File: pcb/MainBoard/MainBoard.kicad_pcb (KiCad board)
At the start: 2 copper layers, 47 parts, among them P1 Camera pot 1, P2 Camera pot 2, P3 Motor controller, P4 Motor battery, P5 Steering connector, P6 Arduino battery, SW1 OnOffDoubleSwitch, U1 arduino_mini, U2 notgate_74HCT04, U3 arduino_mini

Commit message: PCB design finished
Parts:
- removed C_BULK_1, C_BULK_2, C_BULK_3: 10-100uF, Capacitors_ThroughHole:C_Radial_D6.3_L11.2_P2.5
- removed C_BULK_10, C_BULK_11, C_BULK_4, C_BULK_5, C_BULK_6, C_BULK_7, C_BULK_8, C_BULK_9: 10-100uF, Capacitors_SMD:C_1206_HandSoldering
- removed C_PWR_3, C_PWR_4: C, Capacitors_ThroughHole:C_Radial_D6.3_L11.2_P2.5
- removed U1, U3: arduino_mini, arduino:arduino_mini
- removed U2: notgate_74HCT04, Housings_SOIC:SOIC-14_3.9x8.7mm_Pitch1.27mm
- added ARD1: arduino_mini, arduino:arduino_mini, B.Cu at (79.8, 76.2)
- added ARD2: arduino_mini, arduino:arduino_mini, B.Cu at (114.8, 77.3)
- added C_3VBULK_1: 10-100uF, Capacitors_SMD:C_1206_HandSoldering, B.Cu at (90.7, 50.7)
- added C_3VBULK_2: 10-100uF, Capacitors_SMD:C_1206_HandSoldering, B.Cu at (90.7, 54.3)
- added C_5VBULK_1: 10-100uF, Capacitors_ThroughHole:C_Radial_D6.3_L11.2_P2.5, B.Cu at (131.9, 77.3)
- added C_5VBULK_2: 10-100uF, Capacitors_SMD:C_1206_HandSoldering, F.Cu at (114.5, 93.3)
- added C_5VBULK_3: 10-100uF, Capacitors_SMD:C_1206_HandSoldering, F.Cu at (114.6, 87.9)
- added NOT1: notgate_74HCT04, Housings_SOIC:SOIC-14_3.9x8.7mm_Pitch1.27mm, F.Cu at (96.6, 60.8)
- added REF**: 1pin, Connect:1pin, F.Cu at (152.1, 103.0)
- added REF**: 1pin, Connect:1pin, F.Cu at (152.1, 53.1)
- added REF**: 1pin, Connect:1pin, F.Cu at (72.1, 53.1)
- added REF**: 1pin, Connect:1pin, F.Cu at (72.1, 103.0)
- C_CAM_1, C_FIFO_2, C_NOT_1, C_PWR_1, C_PWR_2, C_SH_2, C_TFT_1, DCDC2, DCDC3, FIFO2, LS1, SH1: moved to B.Cu
- moved C_CAM_1 76.2 mm to (78.9, 73.9), turned to 180 degrees
- moved R2 75.8 mm to (76.8, 80.4), turned to 90 degrees
- moved OV76701 75.6 mm to (81.1, 70.9), turned to 180 degrees
- moved C_TFT_1 73.4 mm to (75.7, 95.9), turned to 270 degrees
- moved R1 72.8 mm to (80.0, 80.4), turned to 90 degrees
- moved LS1 71.8 mm to (79.9, 83.7), turned to 180 degrees
- moved C_LS_1 69.7 mm to (83.2, 80.6), turned to 270 degrees
- moved C_NOT_1 69.0 mm to (95.4, 61.0)
- moved TFT1 67.7 mm to (81.1, 98.9), turned to 180 degrees
- moved P3 63.8 mm to (113.7, 51.5), turned to 270 degrees
- moved FIFO2 59.5 mm to (94.7, 79.5)
- moved C_SH_2 58.8 mm to (89.8, 101.2), turned to 180 degrees
- moved FIFO1 55.2 mm to (99.5, 79.5), turned to 180 degrees
- moved SH2 54.7 mm to (94.8, 94.8), turned to 180 degrees
- moved P2 53.9 mm to (94.6, 105.1), turned to 270 degrees
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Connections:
- C_PWR_2 pad 1: Net-(C_PWR_1-Pad1) -> Net-(C_PWR_2-Pad1)
- C_PWR_2 pad 2: Net-(C_PWR_1-Pad2) -> Net-(C_PWR_2-Pad2)
- DCDC3 pad 1: Net-(C_PWR_3-Pad1) -> Net-(C_PWR_2-Pad1)
- DCDC3 pad 2: Net-(C_PWR_3-Pad2) -> Net-(C_PWR_2-Pad2)
- P6 pad 1: Net-(C_PWR_3-Pad2) -> Net-(C_PWR_2-Pad2)
- SW1 pad 6: Net-(C_PWR_3-Pad1) -> Net-(C_PWR_2-Pad1)
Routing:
- net GND: track 0.00 -> 160.9 mm, vias 0 -> 21
- net Net-(ARD1-Pad2): track 0.00 -> 85.5 mm, vias 0 -> 6
- net Net-(ARD1-Pad10): track 0.00 -> 64.8 mm
- net /SectionCommBuffer/FIFO_POP: track 0.00 -> 63.7 mm, vias 0 -> 3
- net +5V: track 0.00 -> 60.2 mm, vias 0 -> 8
- net Net-(ARD1-Pad11): track 0.00 -> 56.0 mm
- net Net-(C_PWR_1-Pad1): track 0.00 -> 54.4 mm
- net Net-(C_PWR_2-Pad1): track 0.00 -> 48.5 mm
- net Net-(FIFO1-Pad3): track 0.00 -> 47.4 mm, vias 0 -> 1
- net /Sheet57F22415/Pixel_D0: track 0.00 -> 42.7 mm
- net /Sheet57F22415/Pixel_D1: track 0.00 -> 41.8 mm
- net /Sheet57F22415/SPI_CLOCK: track 0.00 -> 41.6 mm, vias 0 -> 1
- net Net-(DCDC1-Pad4): track 0.00 -> 40.0 mm
- net /SectionMainControl/STEERING: track 0.00 -> 38.8 mm
- net /SectionMainControl/FORWARD: track 0.00 -> 38.8 mm
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- added copper zone on F.Cu, net +5V
- added copper zone on B.Cu, net GND
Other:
- board outline added: 90 x 60 mm
- board text added: "+ -"
- board text added: "- + S"
- board text added: "CPU"
- board text added: "Motors"

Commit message: generated gerber files
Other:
- board text added: "v1.0"
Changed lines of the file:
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@@
     (area 66.980999 47.398 160.1552 110.041)
     (thickness 1.6)
-    (drawings 12)
+    (drawings 13)
     (tracks 820)
     (zones 0)
@@
     (visible_elements 7FFFFFFF)
     (pcbplotparams
-      (layerselection 0x00030_80000001)
-      (usegerberextensions false)
+      (layerselection 0x010f0_80000001)
+      (usegerberextensions true)
       (excludeedgelayer true)
       (linewidth 0.100000)
@@
       (outputformat 1)
       (mirror false)
-      (drillshape 1)
+      (drillshape 0)
       (scaleselection 1)
-      (outputdirectory ""))
+      (outputdirectory gerber/))
   )
   (net 0 "")
@@
     )
   )
+  (gr_text v1.0 (at 80.1624 105.6894) (layer F.SilkS)
+    (effects (font (size 1.5 1.5) (thickness 0.3)))
+  )
   (gr_text "- + S" (at 114.8461 102.3874) (layer F.SilkS)

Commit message: fixed power module ground connections
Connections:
- C_PWR_1 pad 2: Net-(C_PWR_1-Pad2) -> GND
- C_PWR_2 pad 2: Net-(C_PWR_2-Pad2) -> GND
- DCDC1 pad 2: Net-(C_PWR_1-Pad2) -> GND
- DCDC1 pad 4: Net-(DCDC1-Pad4) -> GND
- DCDC2 pad 2: Net-(C_PWR_1-Pad2) -> GND
- DCDC2 pad 4: Net-(DCDC2-Pad4) -> GND
- DCDC3 pad 2: Net-(C_PWR_2-Pad2) -> GND
- P3 pad 3: Net-(DCDC1-Pad4) -> GND
- P4 pad 1: Net-(C_PWR_1-Pad2) -> GND
- P5 pad 3: Net-(DCDC2-Pad4) -> GND
- P6 pad 1: Net-(C_PWR_2-Pad2) -> GND
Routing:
- net GND: track 160.9 -> 289.6 mm
- net Net-(DCDC1-Pad4): track 40.0 -> 0.00 mm
- net Net-(C_PWR_1-Pad2): track 34.7 -> 0.00 mm
- net Net-(DCDC2-Pad4): track 31.5 -> 0.00 mm
- net Net-(C_PWR_2-Pad2): track 22.5 -> 0.00 mm
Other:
- board text added: "v1.1"
- board text removed: "v1.0"

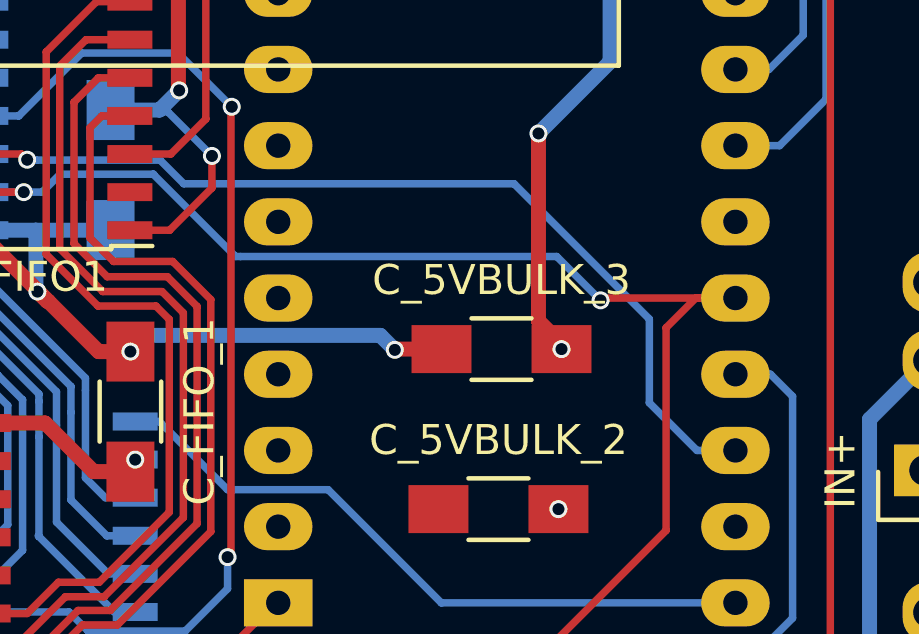
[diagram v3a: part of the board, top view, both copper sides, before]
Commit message: re-assigned data ready from pin 10 to pin 7.
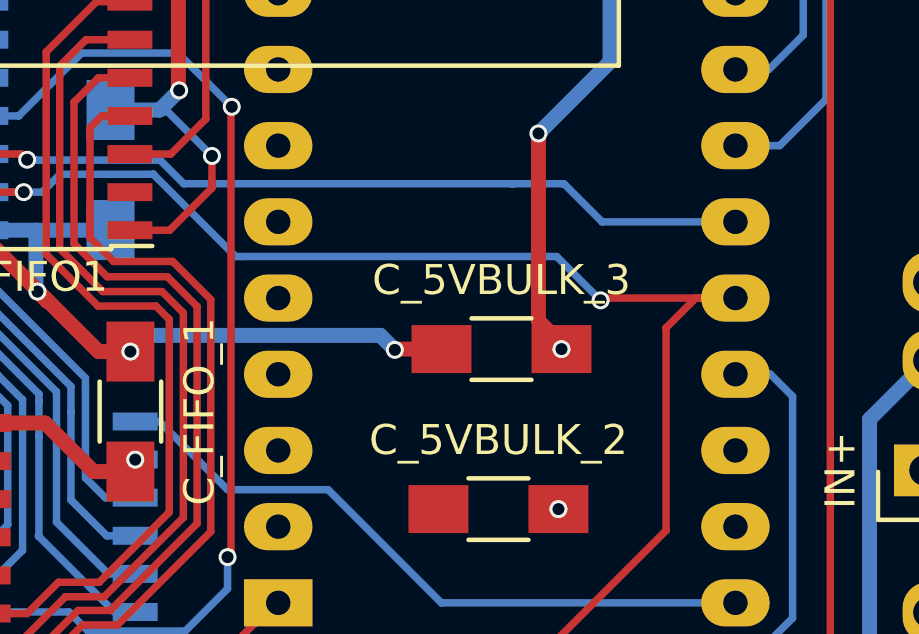
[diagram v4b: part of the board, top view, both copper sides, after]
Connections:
- ARD2 pad 25: Net-(ARD2-Pad25) -> /SectionCommBuffer/DATA_READY
- ARD2 pad 28: /SectionCommBuffer/DATA_READY -> Net-(ARD2-Pad28)
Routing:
- net /SectionCommBuffer/DATA_READY: track 31.3 -> 26.6 mm
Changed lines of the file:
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@@
     (thickness 1.6)
     (drawings 13)
-    (tracks 820)
+    (tracks 822)
     (zones 0)
     (modules 43)
@@
   (net 96 "Net-(ARD2-Pad20)")
   (net 97 "Net-(ARD2-Pad22)")
-  (net 98 "Net-(ARD2-Pad25)")
-  (net 99 "Net-(ARD2-Pad29)")
-  (net 100 "Net-(C_PWR_2-Pad1)")
+  (net 98 "Net-(ARD2-Pad29)")
+  (net 99 "Net-(C_PWR_2-Pad1)")
+  (net 100 "Net-(ARD2-Pad28)")
   (net_class Default "This is the default net class."
     (clearance 0.2)
@@
     (add_net "Net-(ARD2-Pad20)")
     (add_net "Net-(ARD2-Pad22)")
-    (add_net "Net-(ARD2-Pad25)")
+    (add_net "Net-(ARD2-Pad28)")
     (add_net "Net-(ARD2-Pad29)")
     (add_net "Net-(ARD2-Pad3)")
@@
       (net 1 GND))
     (pad 1 thru_hole rect (at 0 0 180) (size 1.3 1.3) (drill 0.8) (layers *.Cu *.Mask B.SilkS)
-      (net 100 "Net-(C_PWR_2-Pad1)"))
+      (net 99 "Net-(C_PWR_2-Pad1)"))
     (model Capacitors_ThroughHole.3dshapes/C_Radial_D6.3_L11.2_P2.5.wrl
       (at (xyz 0 0 0))
@@
       (net 1 GND))
     (pad 1 thru_hole rect (at -6.3 -20.4 270) (size 2.032 1.7272) (drill 1.016) (layers *.Cu *.Mask B.SilkS)
-      (net 100 "Net-(C_PWR_2-Pad1)"))
+      (net 99 "Net-(C_PWR_2-Pad1)"))
   )
   (module Housings_SOIC:SOIC-16_3.9x9.9mm_Pitch1.27mm (layer F.Cu)
@@
       (net 62 "Net-(SW1-Pad1)"))
     (pad 6 thru_hole oval (at 2.9 -0.1) (size 2.032 1.7272) (drill 1.016) (layers *.Cu *.Mask F.SilkS)
-      (net 100 "Net-(C_PWR_2-Pad1)"))
+      (net 99 "Net-(C_PWR_2-Pad1)"))
     (pad 5 thru_hole oval (at 2.9 2.44) (size 2.032 1.7272) (drill 1.016) (layers *.Cu *.Mask F.SilkS)
       (net 7 "Net-(D2-Pad1)"))
@@
       (net 51 /SectionMainControl/FORWARD))
     (pad 25 thru_hole oval (at -6.35 7.62 90) (size 1.5748 2.286) (drill 0.8128) (layers *.Cu *.Mask B.SilkS)
-      (net 98 "Net-(ARD2-Pad25)"))
+      (net 20 /SectionCommBuffer/DATA_READY))
     (pad 26 thru_hole oval (at -8.89 7.62 90) (size 1.5748 2.286) (drill 0.8128) (layers *.Cu *.Mask B.SilkS)
       (net 21 /SectionCommBuffer/FIFO_POP))
@@
       (net 59 /SectionMainControl/FIFO_ENABLE))
     (pad 28 thru_hole oval (at -13.97 7.62 90) (size 1.5748 2.286) (drill 0.8128) (layers *.Cu *.Mask B.SilkS)
-      (net 20 /SectionCommBuffer/DATA_READY))
+      (net 100 "Net-(ARD2-Pad28)"))
     (pad 29 thru_hole oval (at -16.51 7.62 90) (size 1.5748 2.286) (drill 0.8128) (layers *.Cu *.Mask B.SilkS)
-      (net 99 "Net-(ARD2-Pad29)"))
+      (net 98 "Net-(ARD2-Pad29)"))
     (pad 30 thru_hole oval (at -19.05 7.62 90) (size 1.5748 2.286) (drill 0.8128) (layers *.Cu *.Mask B.SilkS)
       (net 58 /SectionMainControl/SPI_DATA_IN))
@@
   (segment (start 95.0976 81.1022) (end 96.0374 80.1624) (width 0.25) (layer F.Cu) (net 19))
   (segment (start 95.0976 81.1022) (end 95.0976 84.201) (width 0.25) (layer F.Cu) (net 19))
-  (segment (start 99.0981 81.6356) (end 98.806 81.6356) (width 0.25) (layer B.Cu) (net 20))
-  (segment (start 121.1199 91.313) (end 119.5324 89.7255) (width 0.25) (layer B.Cu) (net 20))
-  (segment (start 119.5324 89.7255) (end 119.5324 86.9315) (width 0.25) (layer B.Cu) (net 20))
-  (segment (start 119.5324 86.9315) (end 115.0239 82.423) (width 0.25) (layer B.Cu) (net 20))
-  (segment (start 115.0239 82.423) (end 104.013 82.423) (width 0.25) (layer B.Cu) (net 20))
-  (segment (start 104.013 82.423) (end 103.2256 81.6356) (width 0.25) (layer B.Cu) (net 20))
-  (segment (start 103.2256 81.6356) (end 99.0981 81.6356) (width 0.25) (layer B.Cu) (net 20))
-  (segment (start 122.4026 91.313) (end 121.1199 91.313) (width 0.25) (layer B.Cu) (net 20))
+  (segment (start 116.6241 82.423) (end 116.6876 82.423) (width 0.25) (layer B.Cu) (net 20))
+  (segment (start 114.9477 82.423) (end 116.6241 82.423) (width 0.25) (layer B.Cu) (net 20))
+  (segment (start 117.9576 83.693) (end 122.4026 83.693) (width 0.25) (layer B.Cu) (net 20))
+  (segment (start 116.6876 82.423) (end 117.9576 83.693) (width 0.25) (layer B.Cu) (net 20))
+  (segment (start 122.3899 83.6803) (end 122.4026 83.693) (width 0.25) (layer B.Cu) (net 20))
   (segment (start 98.6028 81.4324) (end 96.8172 81.4324) (width 0.25) (layer F.Cu) (net 20))
   (segment (start 98.7933 81.6229) (end 98.6028 81.4324) (width 0.25) (layer F.Cu) (net 20))
   (via (at 98.7933 81.6229) (size 0.6) (drill 0.4) (layers F.Cu B.Cu) (net 20))
   (segment (start 98.806 81.6356) (end 98.7933 81.6229) (width 0.25) (layer B.Cu) (net 20))
+  (segment (start 99.0981 81.6356) (end 98.806 81.6356) (width 0.25) (layer B.Cu) (net 20))
+  (segment (start 115.0239 82.423) (end 114.9477 82.423) (width 0.25) (layer B.Cu) (net 20))
+  (segment (start 114.9477 82.423) (end 104.013 82.423) (width 0.25) (layer B.Cu) (net 20))
+  (segment (start 104.013 82.423) (end 103.2256 81.6356) (width 0.25) (layer B.Cu) (net 20))
+  (segment (start 103.2256 81.6356) (end 99.0981 81.6356) (width 0.25) (layer B.Cu) (net 20))
   (segment (start 105.9053 84.8487) (end 105.7402 84.8487) (width 0.25) (layer B.Cu) (net 21))
   (segment (start 117.9068 86.3092) (end 117.983 86.233) (width 0.25) (layer F.Cu) (net 21))
@@
   (segment (start 86.3092 95.25) (end 87.376 95.25) (width 0.25) (layer B.Cu) (net 80))
   (segment (start 81.0768 63.2714) (end 81.1022 63.2714) (width 0.25) (layer B.Cu) (net 80))
-  (segment (start 148.209 77.5716) (end 148.209 81.6102) (width 0.5) (layer B.Cu) (net 100))
-  (segment (start 141.9336 98.325) (end 140.4918 98.325) (width 0.5) (layer B.Cu) (net 100))
-  (segment (start 149.1996 91.059) (end 141.9336 98.325) (width 0.5) (layer B.Cu) (net 100))
-  (segment (start 149.1996 82.6008) (end 149.1996 91.059) (width 0.5) (layer B.Cu) (net 100))
-  (segment (start 148.209 81.6102) (end 149.1996 82.6008) (width 0.5) (layer B.Cu) (net 100))
-  (segment (start 148.209 77.5716) (end 148.209 72.6948) (width 0.5) (layer B.Cu) (net 100))
-  (segment (start 149.6568 59.4568) (end 146.7396 56.5396) (width 0.5) (layer B.Cu) (net 100))
-  (segment (start 149.6568 71.247) (end 149.6568 59.4568) (width 0.5) (layer B.Cu) (net 100))
-  (segment (start 148.209 72.6948) (end 149.6568 71.247) (width 0.5) (layer B.Cu) (net 100))
+  (segment (start 148.209 77.5716) (end 148.209 81.6102) (width 0.5) (layer B.Cu) (net 99))
+  (segment (start 141.9336 98.325) (end 140.4918 98.325) (width 0.5) (layer B.Cu) (net 99))
+  (segment (start 149.1996 91.059) (end 141.9336 98.325) (width 0.5) (layer B.Cu) (net 99))
+  (segment (start 149.1996 82.6008) (end 149.1996 91.059) (width 0.5) (layer B.Cu) (net 99))
+  (segment (start 148.209 81.6102) (end 149.1996 82.6008) (width 0.5) (layer B.Cu) (net 99))
+  (segment (start 148.209 77.5716) (end 148.209 72.6948) (width 0.5) (layer B.Cu) (net 99))
+  (segment (start 149.6568 59.4568) (end 146.7396 56.5396) (width 0.5) (layer B.Cu) (net 99))
+  (segment (start 149.6568 71.247) (end 149.6568 59.4568) (width 0.5) (layer B.Cu) (net 99))
+  (segment (start 148.209 72.6948) (end 149.6568 71.247) (width 0.5) (layer B.Cu) (net 99))
   (zone (net 1) (net_name GND) (layer B.Cu) (hatch edge 0.508)
     (connect_pads (clearance 0.508))
